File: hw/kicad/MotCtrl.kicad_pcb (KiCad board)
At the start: 4 copper layers, 137 parts, among them P1 CONN_01X06, P2 CONN_01X03, P3 CONN_02X05, P4 CONN_01X05, Q1 FDBL0110N60, Q2 FDBL0110N60, Q3 FDBL0110N60, Q4 FDBL0110N60, Q5 FDBL0110N60, Q6 FDBL0110N60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

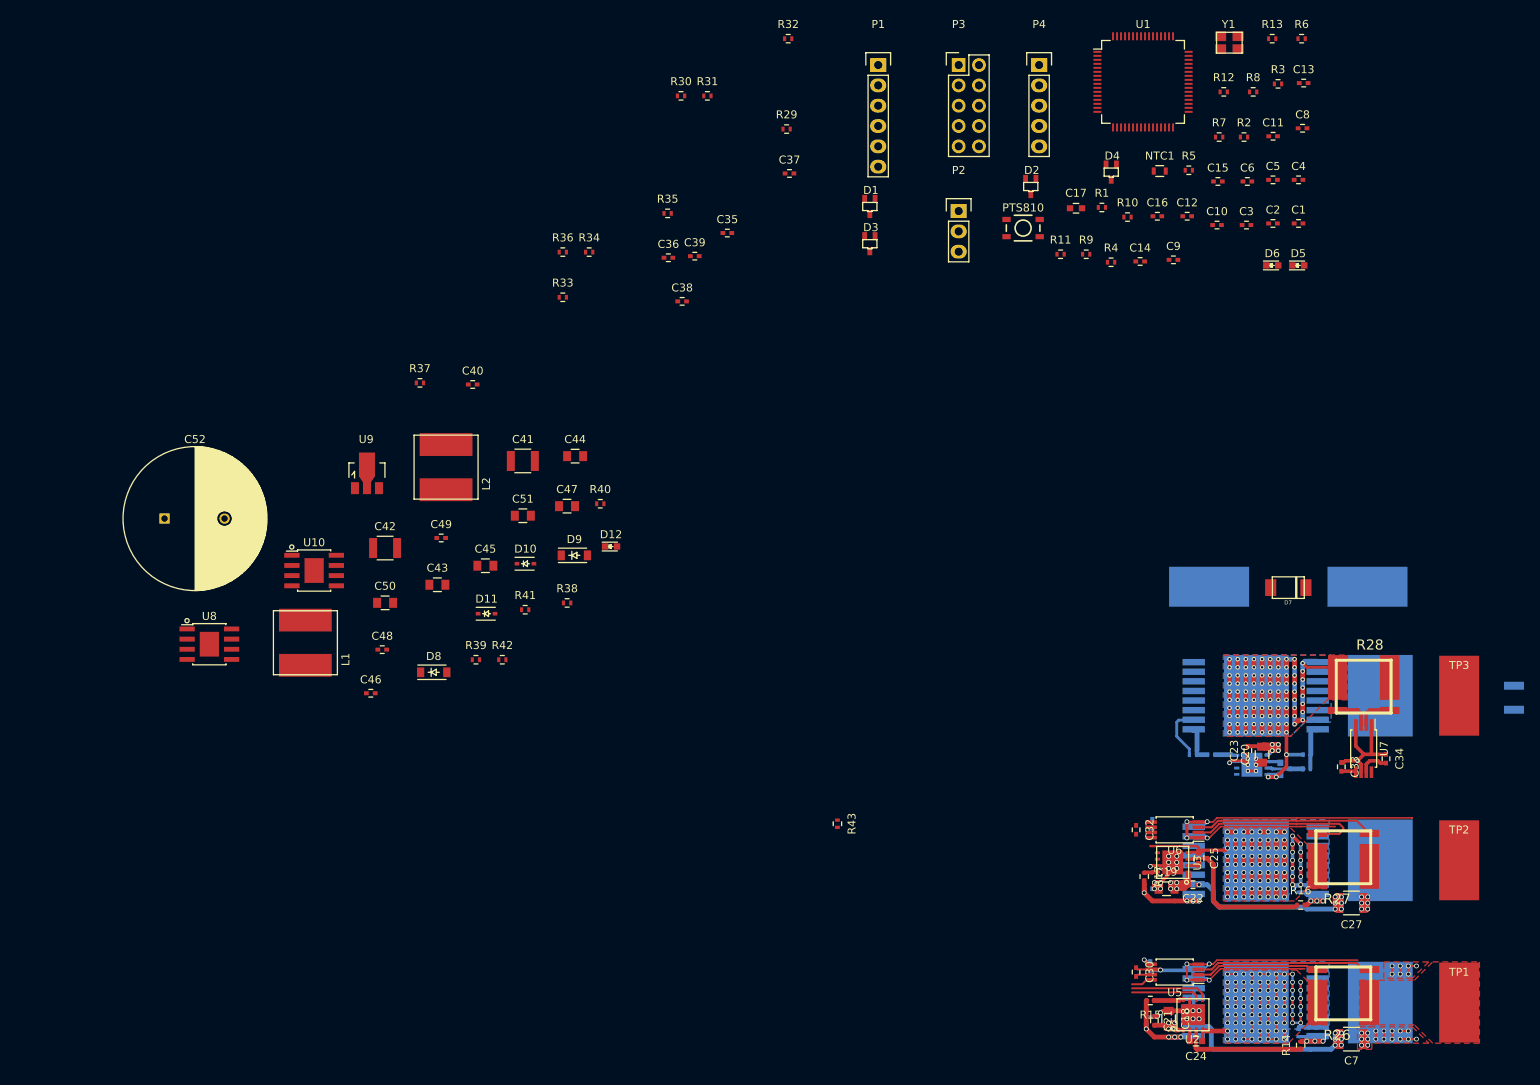
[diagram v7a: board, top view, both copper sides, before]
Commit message: Started duplicating and aligning power stages
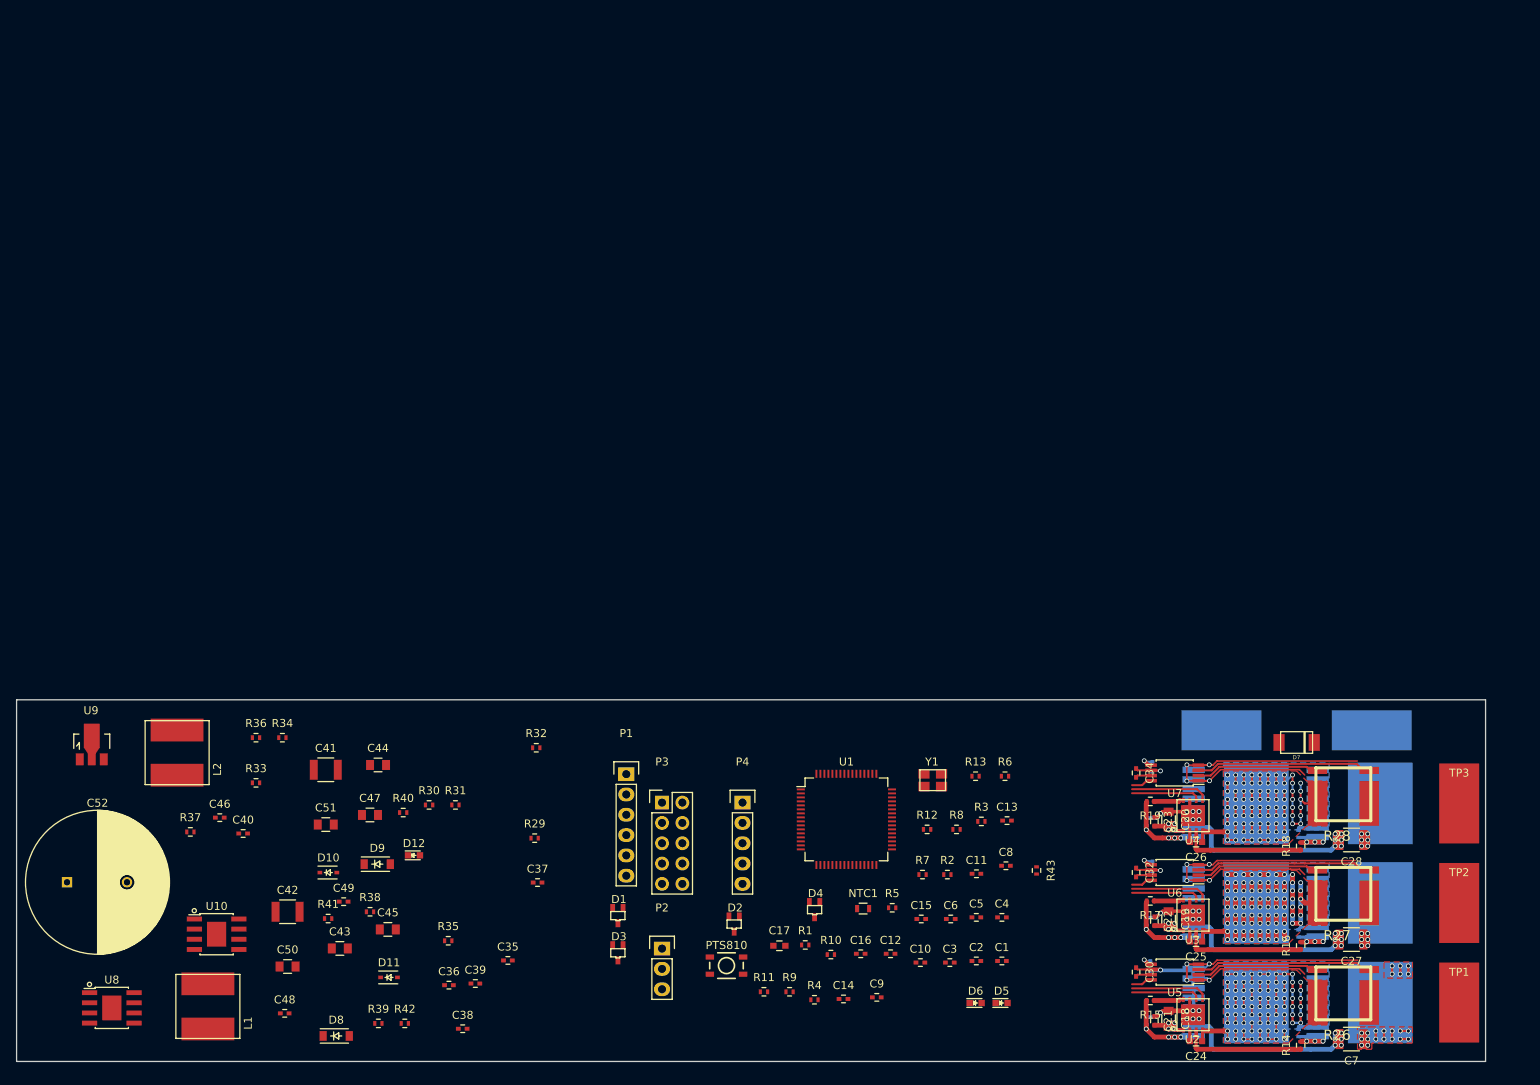
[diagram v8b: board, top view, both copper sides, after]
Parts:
- C26, C28, R18, R19, U4: moved to F.Cu
- C33: moved to B.Cu
- moved C4 99.4 mm to (143.5, 133.6)
- moved C5 99.4 mm to (140.3, 133.6)
- moved C9 99.4 mm to (127.9, 143.6)
- moved C1 99.4 mm to (143.5, 139.1)
- moved C11 99.4 mm to (140.3, 128.2)
- moved C12 99.4 mm to (129.6, 138.2)
- moved C13 99.4 mm to (144.1, 121.5)
- moved C14 99.4 mm to (123.7, 143.8)
- moved C15 99.4 mm to (133.4, 133.8)
- moved C16 99.4 mm to (125.8, 138.2)
- moved C17 99.4 mm to (115.7, 137.2)
- moved C2 99.4 mm to (140.3, 139.1)
- moved C6 99.4 mm to (137.1, 133.8)
- moved C8 99.4 mm to (144.0, 127.2)
- moved D2 99.4 mm to (110.0, 134.5)
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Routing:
- net GND: track 240.8 -> 297.1 mm, vias 48 -> 54
- net /Power FET/MOT_PH_C: track 21.4 -> 0.00 mm, vias 17 -> 0
- net VPP: track 62.6 -> 82.4 mm, vias 30 -> 34
- net Net-(R28-Pad4): track 4.69 -> 22.2 mm
- net +12V: track 51.2 -> 38.7 mm
- net /Power FET/PH_C: track 107.5 -> 118.7 mm, vias 83 -> 85
- net Net-(R18-Pad1): track 4.55 -> 15.5 mm
- net Net-(R28-Pad3): track 4.69 -> 15.6 mm
- net /Microcontroller/PWM_H_C: track 0.00 -> 9.82 mm
- net /Microcontroller/PWM_H_B: track 0.00 -> 9.82 mm
- net /Microcontroller/PWM_L_C: track 0.00 -> 8.68 mm
- net /Microcontroller/PWM_L_B: track 0.00 -> 8.68 mm
- net /Power FET/PH_B: track 111.8 -> 120.1 mm
- net Net-(Q6-Pad1): track 5.42 -> 13.8 mm, vias 0 -> 4
- net Net-(R27-Pad3): track 22.6 -> 15.6 mm
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- added copper zone on B.Cu, net /Power FET/PH_C
- added copper zone on F.Cu, net /Power FET/PH_C
- removed copper zone on F.Cu, net /Power FET/MOT_PH_A
- removed copper zone on B.Cu, net Net-(C26-Pad1)
- removed copper zone on F.Cu, net Net-(C26-Pad1)
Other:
- board outline added: 183.6 x 45.2 mm
